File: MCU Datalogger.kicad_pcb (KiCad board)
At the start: 2 copper layers, 49.5 x 26.5 mm, 29 parts, among them J1 Conn_01x04_Pin, J2 Conn_01x04_Pin, J3 Conn_01x09_Pin, J4 Conn_02x03_Odd_Even, U1 24LC1025, U2 24LC1025, U3 DS1337S_, U4 ATMEGA328P-AU, Y1 16 MHz, Y2 32.768kHz

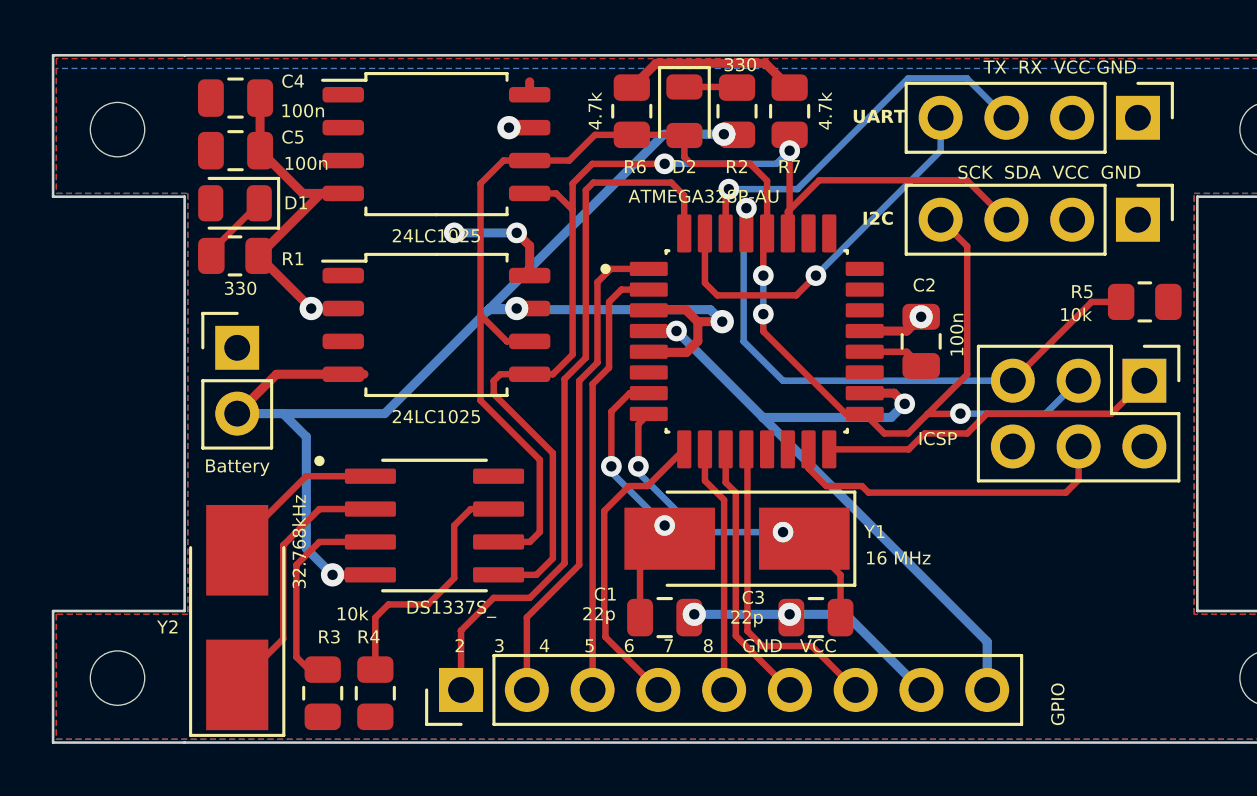
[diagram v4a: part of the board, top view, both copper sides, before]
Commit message: Logos and informations added
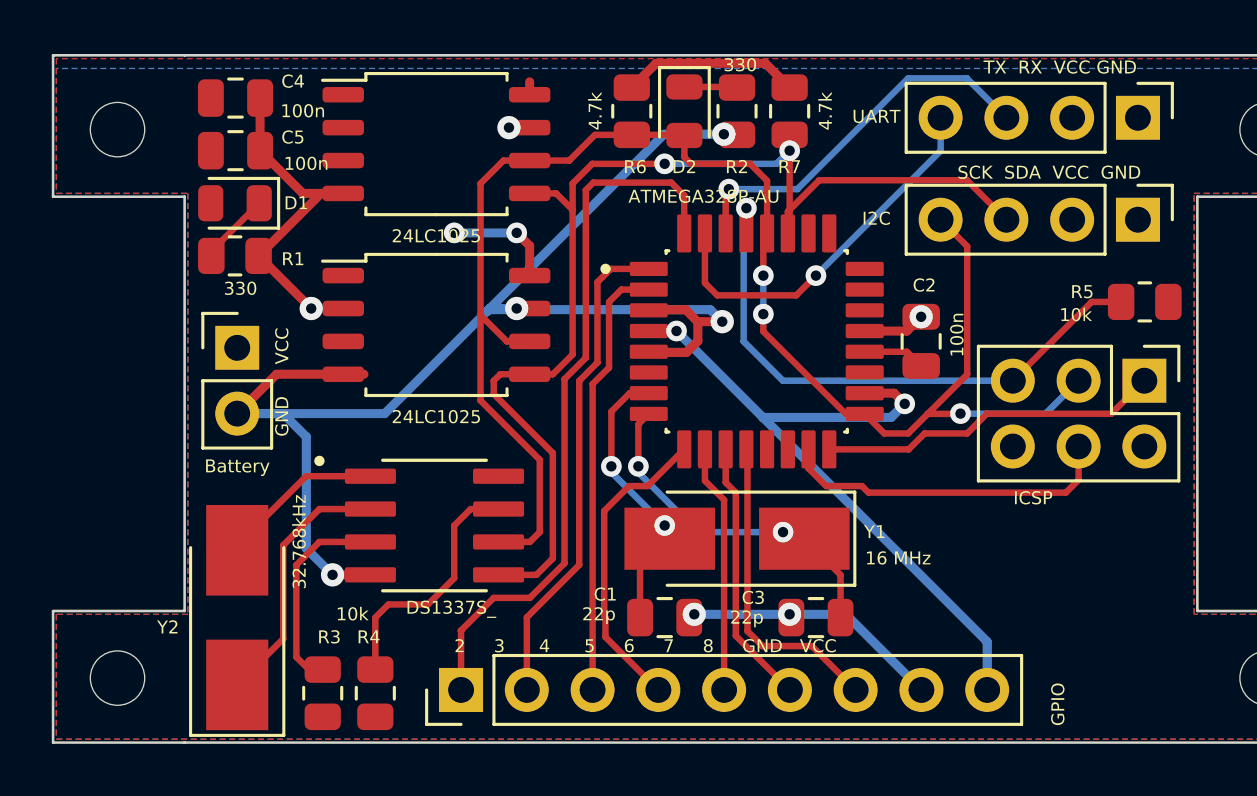
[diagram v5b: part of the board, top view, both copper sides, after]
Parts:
- added REF**: KiCad-Logo2_5mm_SilkScreen, Symbol:KiCad-Logo2_5mm_SilkScreen, B.Cu at (138.9, 54.0)
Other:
- board text added: "-2Mbit EEPROM -RTC -I2C, SPI,GPIO"
- board text added: "Data logger with ATMEGA328"
- board text added: "GND"
- board text added: "VCC"

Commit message: Completed 2-laye PCB project
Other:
- board text added: "0.2000 mm / 0.0000 mm"
- board text added: "0.3000 mm"
- board text added: "1.6000 mm"
- board text added: "2"
- board text added: "49.5300 mm x 26.5430 mm"
- board text added: "BOARD CHARACTERISTICS"
- board text added: "Board Thickness:"
- board text added: "Board overall dimensions:"
- board text added: "Castellated pads:"
- board text added: "Copper Finish:"
- board text added: "Copper Layer Count:"
- board text added: "Edge card connectors:"
- board text added: "Impedance Control:"
- board text added: "Min hole diameter:"
- board text added: "Min track/spacing:"
- board text added: "No"
- board text added: "None"
- board text added: "Plated Board Edge:"
